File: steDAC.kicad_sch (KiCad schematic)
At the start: 17 parts

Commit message: Adding Initial MCU configuration
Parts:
- removed C1, C3, C5, C? (x4): 0.1u, symbol Device:C_Small
- removed C2, C4, C? (x5): 10u, symbol Device:C_Polarized_Small_US
- removed C6, C?: 470u, symbol Device:C_Polarized_Small_US
- removed U?: AK4493, symbol steDAC:AK4493
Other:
- added sheet AK4493 interface (AK4493_sch.kicad_sch)
- added sheet MCU interface (MCU_sch.kicad_sch)

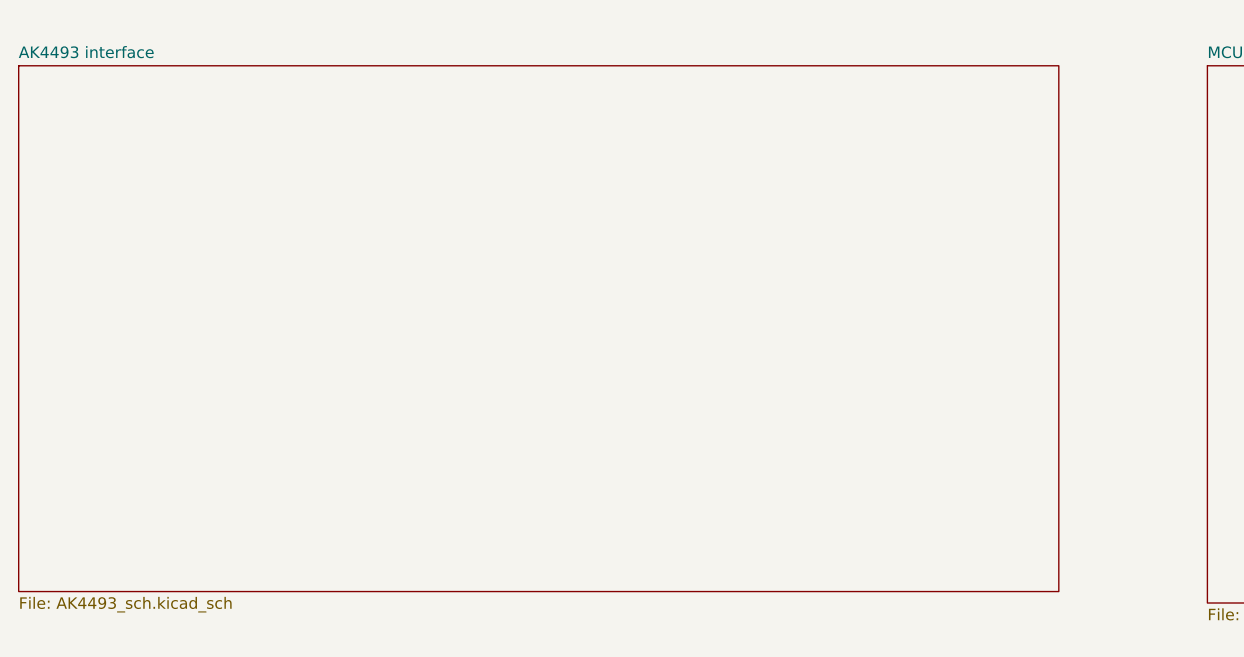
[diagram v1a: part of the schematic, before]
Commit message: Adding ES9038 parts
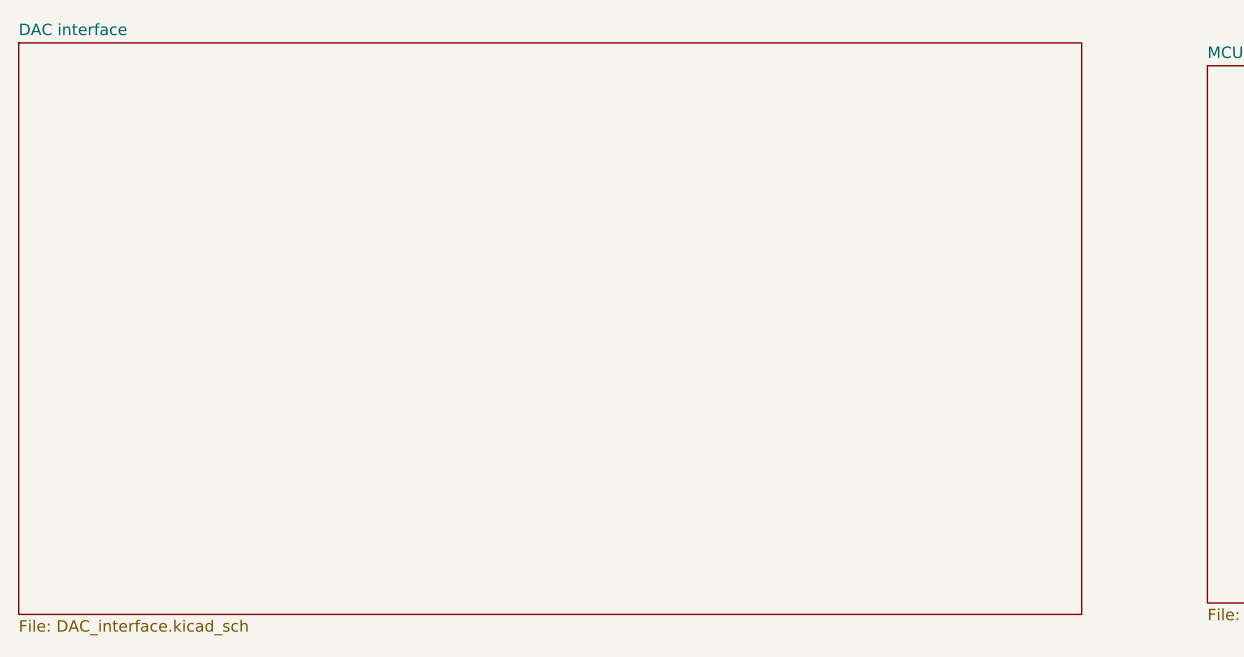
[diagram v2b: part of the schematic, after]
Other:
- removed sheet AK4493 interface
- added sheet DAC interface (DAC_interface.kicad_sch)
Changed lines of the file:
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@@
     (title "AK4493 Interface")
   )
-  (sheet (at 22.86 22.86) (size 115.57 58.42) (fields_autoplaced)
+  (sheet (at 22.86 20.32) (size 118.11 63.5) (fields_autoplaced)
     (stroke (width 0.1524) (type solid) (color 0 0 0 0))
     (fill (color 0 0 0 0.0000))
-    (property "Sheet name" "AK4493 interface" (id 0) (at 22.86 22.1484 0)
+    (property "Sheet name" "DAC interface" (id 0) (at 22.86 19.6084 0)
       (effects (font (size 1.27 1.27)) (justify left bottom))
     )
-    (property "Sheet file" "AK4493_sch.kicad_sch" (id 1) (at 22.86 81.8646 0)
+    (property "Sheet file" "DAC_interface.kicad_sch" (id 1) (at 22.86 84.4046 0)
       (effects (font (size 1.27 1.27)) (justify left top))
     )
@@
   (sheet_instances
     (path "/" (page "1"))
-    (path "/8f3ba7be-9a40-49f2-8546-84dae5a13bbf" (page "2"))
+    (path "/19d5df4d-7eb1-4c05-84fc-f97af242e346" (page "3"))
     (path "/b39b8c19-ac96-4230-ae13-d0827749d2e6" (page "3"))
   )
@@
       (reference "#PWR?") (unit 1) (value "+3.3V") (footprint "")
     )
-    (path "/8f3ba7be-9a40-49f2-8546-84dae5a13bbf/34ccdc88-7adc-432a-9a03-1aeda9749954"
-      (reference "#PWR?") (unit 1) (value "GND") (footprint "")
-    )
     (path "/b39b8c19-ac96-4230-ae13-d0827749d2e6/50f65121-91ed-41f4-85ea-5985bb55c161"
       (reference "#PWR?") (unit 1) (value "GND") (footprint "")
@@
       (reference "#PWR?") (unit 1) (value "GND") (footprint "")
     )
-    (path "/8f3ba7be-9a40-49f2-8546-84dae5a13bbf/6a27ac23-2dd7-4303-b9ff-e39948168c4f"
-      (reference "#PWR?") (unit 1) (value "GNDA") (footprint "")
-    )
-    (path "/8f3ba7be-9a40-49f2-8546-84dae5a13bbf/7537ba38-9d06-488b-8837-b08efc97f6a4"
-      (reference "#PWR?") (unit 1) (value "+5VA") (footprint "")
-    )
     (path "/b39b8c19-ac96-4230-ae13-d0827749d2e6/76754a92-43e4-432f-88d4-396c823c1b87"
       (reference "#PWR?") (unit 1) (value "+3.3V") (footprint "")
     )
-    (path "/8f3ba7be-9a40-49f2-8546-84dae5a13bbf/81638e29-0c7e-4d14-a011-8d3adb4148ab"
-      (reference "#PWR?") (unit 1) (value "+5VA") (footprint "")
-    )
-    (path "/8f3ba7be-9a40-49f2-8546-84dae5a13bbf/888bcd7c-c28c-467d-a0df-f2c71731d4f1"
-      (reference "#PWR?") (unit 1) (value "+3.3VA") (footprint "")
-    )
     (path "/b39b8c19-ac96-4230-ae13-d0827749d2e6/9628bbda-14ff-4ab0-aa90-b820950acbf0"
-      (reference "#PWR?") (unit 1) (value "GND") (footprint "")
-    )
-    (path "/8f3ba7be-9a40-49f2-8546-84dae5a13bbf/9fb3ebe2-1975-46b0-9e56-024fdb5dca65"
       (reference "#PWR?") (unit 1) (value "GND") (footprint "")
     )
@@
       (reference "#PWR?") (unit 1) (value "GND") (footprint "")
     )
-    (path "/8f3ba7be-9a40-49f2-8546-84dae5a13bbf/b264f53d-be85-4256-9262-dd49ec6186c0"
-      (reference "#PWR?") (unit 1) (value "GNDA") (footprint "")
-    )
-    (path "/8f3ba7be-9a40-49f2-8546-84dae5a13bbf/b89757a9-7724-450c-b1c9-848367f32584"
-      (reference "#PWR?") (unit 1) (value "+3.3V") (footprint "")
-    )
-    (path "/8f3ba7be-9a40-49f2-8546-84dae5a13bbf/dff174ee-88fe-45ea-aaea-3bf6235c9b9b"
-      (reference "#PWR?") (unit 1) (value "+5V") (footprint "")
-    )
     (path "/b39b8c19-ac96-4230-ae13-d0827749d2e6/f70bdf7f-e24e-4b5a-b74a-bcb3b23c0358"
       (reference "#PWR?") (unit 1) (value "GND") (footprint "")
-    )
-    (path "/8f3ba7be-9a40-49f2-8546-84dae5a13bbf/14816b7f-3927-46cc-9ada-6b0b75a36061"
-      (reference "C?") (unit 1) (value "10u") (footprint "")
     )
     (path "/b39b8c19-ac96-4230-ae13-d0827749d2e6/241371bc-b4d6-4a13-9cfa-ae67d7de870e"
       (reference "C?") (unit 1) (value "0.1u") (footprint "")
     )
-    (path "/8f3ba7be-9a40-49f2-8546-84dae5a13bbf/268b696d-0857-4a4f-8b94-8fe3647e9cef"
-      (reference "C?") (unit 1) (value "10u") (footprint "")
-    )
-    (path "/8f3ba7be-9a40-49f2-8546-84dae5a13bbf/2f090ce6-5b0f-4d4f-be89-2520048e44d0"
-      (reference "C?") (unit 1) (value "10u") (footprint "")
-    )
-    (path "/8f3ba7be-9a40-49f2-8546-84dae5a13bbf/39f574a6-4763-4000-8857-a276ca800ac6"
-      (reference "C?") (unit 1) (value "0.1u") (footprint "")
-    )
-    (path "/8f3ba7be-9a40-49f2-8546-84dae5a13bbf/40dc5062-01d4-4afd-b723-3edbebf43d5d"
-      (reference "C?") (unit 1) (value "0.1u") (footprint "")
-    )
     (path "/b39b8c19-ac96-4230-ae13-d0827749d2e6/41e1ea71-e2d0-4d1e-af63-01d99c5d749a"
       (reference "C?") (unit 1) (value "18u") (footprint "")
-    )
-    (path "/8f3ba7be-9a40-49f2-8546-84dae5a13bbf/43a60bf8-c479-4610-b910-1bd14b736349"
-      (reference "C?") (unit 1) (value "10u") (footprint "")
-    )
-    (path "/8f3ba7be-9a40-49f2-8546-84dae5a13bbf/53891b88-f1a1-4c61-b083-3fcaa127f940"
-      (reference "C?") (unit 1) (value "0.1u") (footprint "")
     )
     (path "/b39b8c19-ac96-4230-ae13-d0827749d2e6/5e755535-eee8-4f70-add8-0ec398f9814f"
@@
       (reference "C?") (unit 1) (value "0.1u") (footprint "")
     )
-    (path "/8f3ba7be-9a40-49f2-8546-84dae5a13bbf/64cdd5f2-2bad-4fdd-b9d5-dcf88b1b7b21"
-      (reference "C?") (unit 1) (value "0.1u") (footprint "")
-    )
-    (path "/8f3ba7be-9a40-49f2-8546-84dae5a13bbf/732ef67b-bdc4-4528-827d-8a9de1961cd1"
-      (reference "C?") (unit 1) (value "0.1u") (footprint "")
-    )
-    (path "/8f3ba7be-9a40-49f2-8546-84dae5a13bbf/7d9f9f66-7378-460b-9da9-21b4575be24a"
-      (reference "C?") (unit 1) (value "470u") (footprint "")
-    )
-    (path "/8f3ba7be-9a40-49f2-8546-84dae5a13bbf/837907ef-463d-4a3e-b64a-151b742336a7"
-      (reference "C?") (unit 1) (value "0.1u") (footprint "")
-    )
-    (path "/8f3ba7be-9a40-49f2-8546-84dae5a13bbf/983fee74-b338-4d55-8966-0ad6d0146cef"
-      (reference "C?") (unit 1) (value "10u") (footprint "")
-    )
-    (path "/8f3ba7be-9a40-49f2-8546-84dae5a13bbf/99b84ca9-a815-485a-a0a9-185c72f07f68"
-      (reference "C?") (unit 1) (value "0.1u") (footprint "")
-    )
-    (path "/8f3ba7be-9a40-49f2-8546-84dae5a13bbf/a59beaac-ad6b-4af7-8712-34460574c822"
-      (reference "C?") (unit 1) (value "10u") (footprint "")
-    )
     (path "/b39b8c19-ac96-4230-ae13-d0827749d2e6/b2d88b91-2abe-4d3c-a4cf-786194e61c0f"
       (reference "C?") (unit 1) (value "0.1u") (footprint "")
-    )
-    (path "/8f3ba7be-9a40-49f2-8546-84dae5a13bbf/c37998ed-e4b9-4cdb-8fed-1e8240a71c1b"
-      (reference "C?") (unit 1) (value "470u") (footprint "")
     )
     (path "/b39b8c19-ac96-4230-ae13-d0827749d2e6/d7f23cec-93af-40ca-b30a-52dc1a1f969d"
       (reference "C?") (unit 1) (value "0.1u") (footprint "")
     )
-    (path "/8f3ba7be-9a40-49f2-8546-84dae5a13bbf/ea66459f-5d13-489c-b90c-3794c93458ec"
-      (reference "C?") (unit 1) (value "10u") (footprint "")
-    )
     (path "/b39b8c19-ac96-4230-ae13-d0827749d2e6/046ebd45-5a1e-458e-8791-c49748f8d85e"
       (reference "IC?") (unit 1) (value "PIC32MX120F032B-I_SP") (footprint "DIP794W56P254L3486H508Q28N")
+    )
+    (path "/19d5df4d-7eb1-4c05-84fc-f97af242e346/dec9d0d6-ee28-476b-be25-eb2806a0e685"
+      (reference "IC?") (unit 1) (value "ES9038Q2M") (footprint "QFN40P300X500X80-31N-D")
     )
     (path "/b39b8c19-ac96-4230-ae13-d0827749d2e6/3698e845-8a5f-4af1-97ef-88d8ce2d353c"
@@
       (reference "R?") (unit 1) (value "1K") (footprint "")
     )
-    (path "/8f3ba7be-9a40-49f2-8546-84dae5a13bbf/1d225dc2-5280-42d8-8e77-6a14174a7ac6"
-      (reference "U?") (unit 1) (value "AK4493") (footprint "")
+    (path "/19d5df4d-7eb1-4c05-84fc-f97af242e346/89dc7f23-ac8d-4ccf-a836-107fd80333da"
+      (reference "Y?") (unit 1) (value "Crystal") (footprint "")
     )
     (path "/b39b8c19-ac96-4230-ae13-d0827749d2e6/f6a9fccb-71db-4d92-b3a9-f05d07461aeb"

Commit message: WIP output stage
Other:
- added sheet Output Stage (output_stage.kicad_sch)
- added sheet Power Supplies (power.kicad_sch)

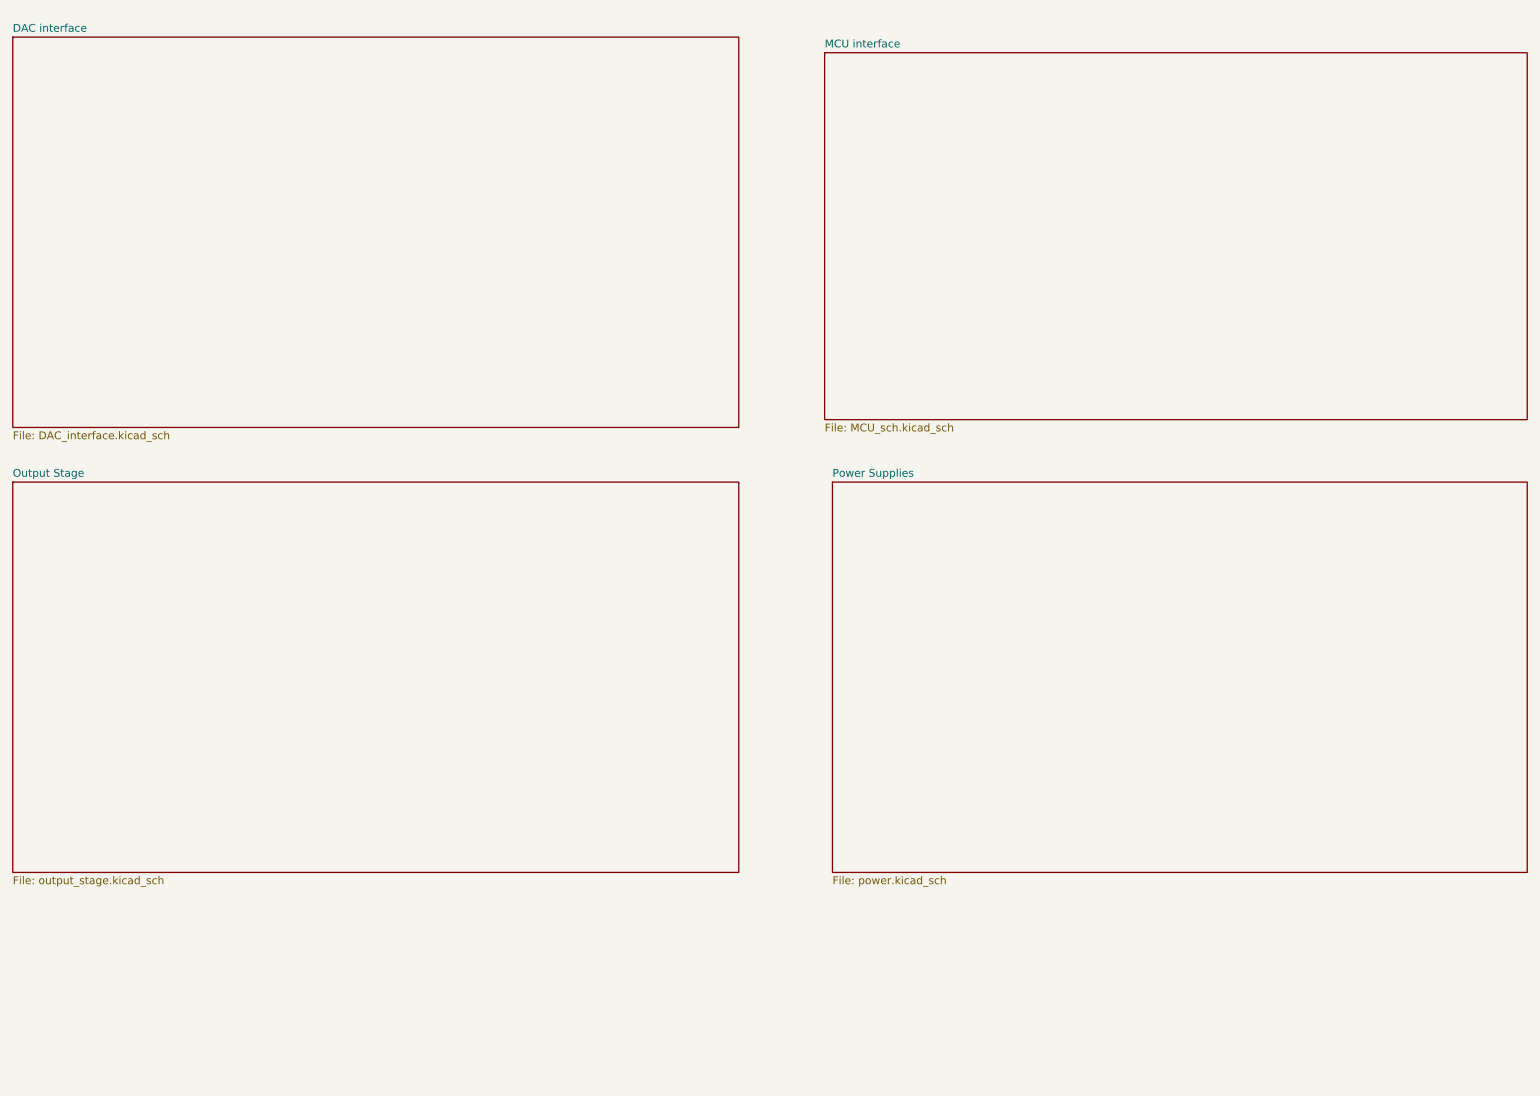
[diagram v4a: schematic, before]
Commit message: Adding values to output stage
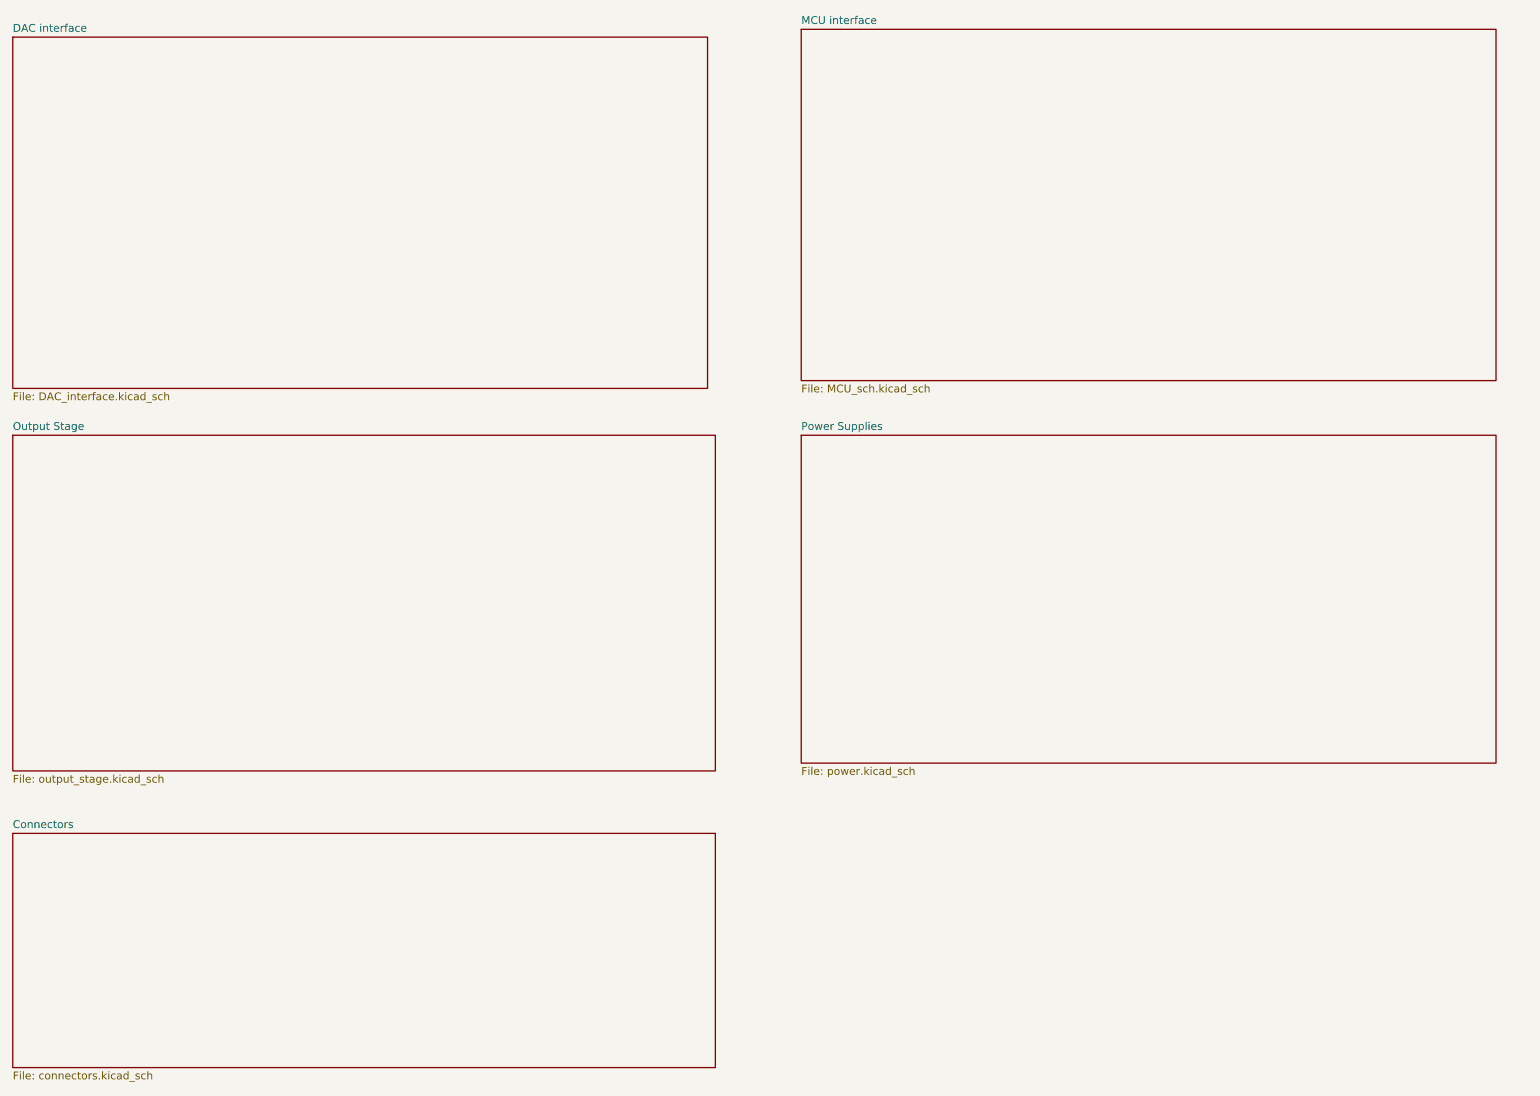
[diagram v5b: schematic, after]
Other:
- added sheet Connectors (connectors.kicad_sch)
- title: AK4493 Interface -> SteDAC overall sheet

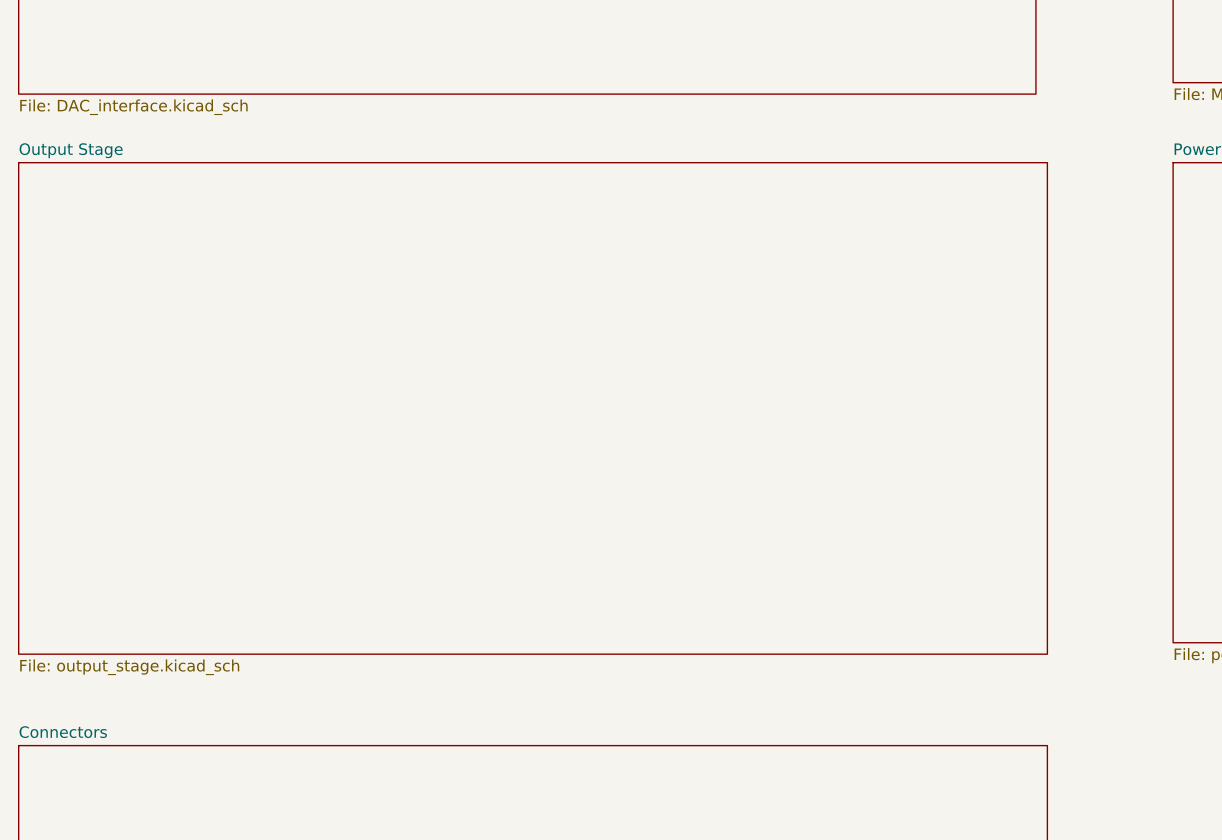
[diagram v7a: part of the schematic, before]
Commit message: Finishing Schematic. Fixed ERC errors
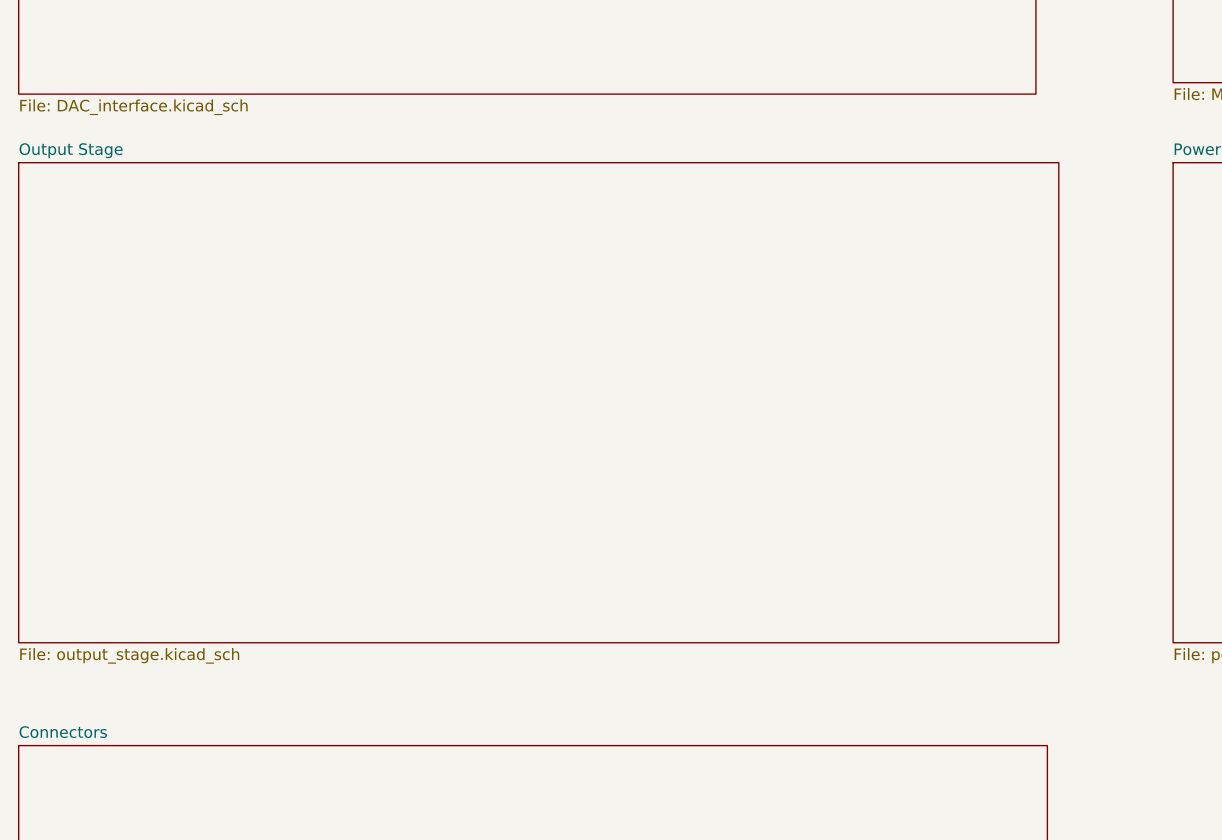
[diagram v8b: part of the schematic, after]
